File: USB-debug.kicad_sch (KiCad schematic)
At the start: 44 parts, among them J4 USB-C_GCT_USB4105-GF-A, Q25 BSS138PW, Q4 BSS138PW, U16 TPD4E05U06QDQARQ1, U31 FT4232H_VQFN, Y2 Oscillator_12MHz_ESC_2520MV

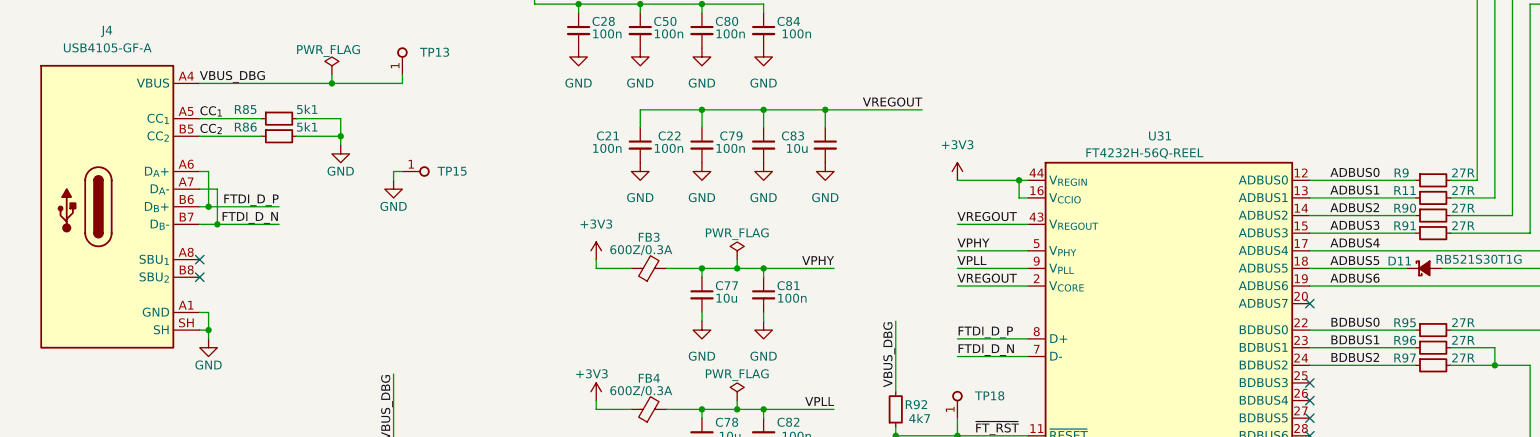
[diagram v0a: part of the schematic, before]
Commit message: Bump to KiCad 9.x
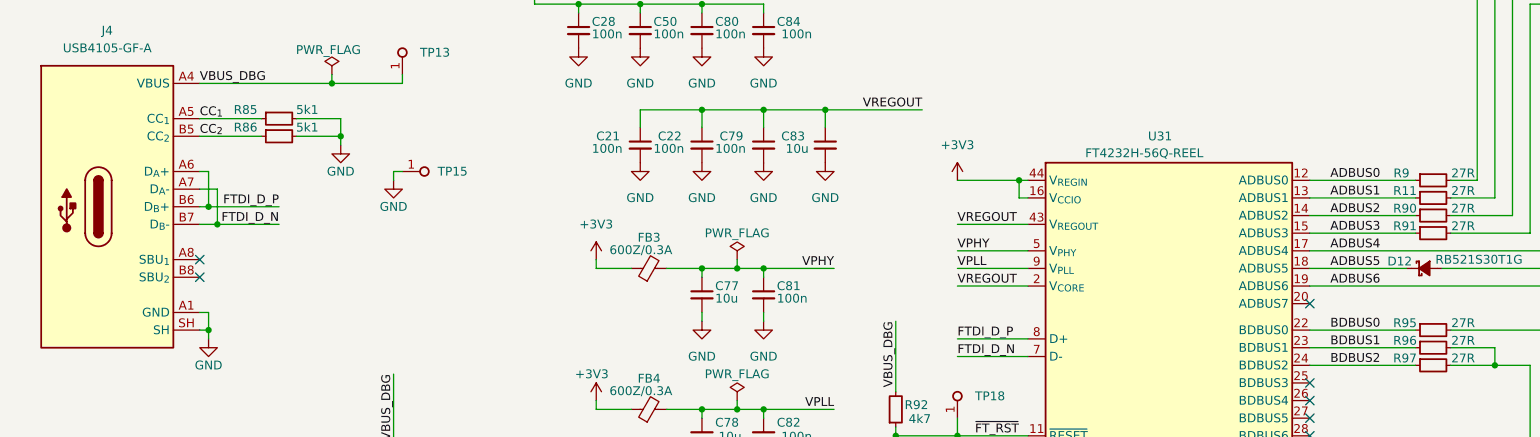
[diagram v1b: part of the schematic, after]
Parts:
- renumbered D11 to D12
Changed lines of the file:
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@@
 (kicad_sch
-	(version 20231120)
+	(version 20250114)
 	(generator "eeschema")
-	(generator_version "8.0")
+	(generator_version "9.0")
 	(paper "A4")
 	(title_block
@@
 		(rev "1.0.0")
 	)
+	(text "FTDI"
+		(exclude_from_sim no)
+		(at 182.626 21.082 0)
+		(effects
+			(font
+				(size 2.54 2.54)
+				(thickness 0.508)
+				(bold yes)
+			)
+		)
+	)
+	(text "Debug USB-C Connector"
+		(exclude_from_sim no)
+		(at 45.466 22.352 0)
+		(effects
+			(font
+				(size 2.54 2.54)
+				(thickness 0.508)
+				(bold yes)
+			)
+		)
+	)
 	(junction
 		(at 115.57 113.03)
@@
 		)
 	)
-	(text "FTDI"
-		(exclude_from_sim no)
-		(at 182.626 21.082 0)
-		(effects
-			(font
-				(size 2.54 2.54)
-				(thickness 0.508)
-				(bold yes)
-			)
-		)
-	)
-	(text "Debug USB-C Connector"
-		(exclude_from_sim no)
-		(at 45.466 22.352 0)
-		(effects
-			(font
-				(size 2.54 2.54)
-				(thickness 0.508)
-				(bold yes)
-			)
-		)
-	)
 	(label "FTDI_D_P"
 		(at 55.88 62.23 180)
-		(fields_autoplaced yes)
 		(effects
 			(font
@@
 	(label "FTDI_D_N"
 		(at 55.88 64.77 180)
-		(fields_autoplaced yes)
 		(effects
 			(font
@@
 	(label "FTDI_D_P"
 		(at 21.59 105.41 0)
-		(fields_autoplaced yes)
 		(effects
 			(font
@@
 	(label "IMU.SCL"
 		(at 248.92 99.06 180)
-		(fields_autoplaced yes)
 		(effects
 			(font
@@
 	(label "FTDI_D_N"
 		(at 153.67 83.82 0)
-		(fields_autoplaced yes)
 		(effects
 			(font
@@
 	(label "~{FT_RST}"
 		(at 156.21 95.25 0)
-		(fields_autoplaced yes)
 		(effects
 			(font
@@
 	(label "VBUS_DBG"
 		(at 144.78 78.74 270)
-		(fields_autoplaced yes)
 		(effects
 			(font
@@
 	(label "VREGOUT"
 		(at 153.67 64.77 0)
-		(fields_autoplaced yes)
 		(effects
 			(font
@@
 	(label "VBUS_DBG"
 		(at 44.45 44.45 0)
-		(fields_autoplaced yes)
 		(effects
 			(font
@@
 	(label "VBUS_DBG"
 		(at 72.39 86.36 270)
-		(fields_autoplaced yes)
 		(effects
 			(font
@@
 	(label "BDBUS2"
 		(at 214.63 85.09 180)
-		(fields_autoplaced yes)
 		(effects
 			(font
@@
 	(label "ADBUS4"
 		(at 214.63 68.58 180)
-		(fields_autoplaced yes)
 		(effects
 			(font
@@
 	(label "BDBUS1"
 		(at 214.63 82.55 180)
-		(fields_autoplaced yes)
 		(effects
 			(font
@@
 	(label "CC_{2}"
 		(at 44.45 52.07 0)
-		(fields_autoplaced yes)
 		(effects
 			(font
@@
 	(label "VPLL"
 		(at 153.67 71.12 0)
-		(fields_autoplaced yes)
 		(effects
 			(font
@@
 	(label "FTDI_D_N"
 		(at 21.59 107.95 0)
-		(fields_autoplaced yes)
 		(effects
 			(font
@@
 	(label "VPLL"
 		(at 135.89 91.44 180)
-		(fields_autoplaced yes)
 		(effects
 			(font
@@
 	(label "FPGA_SPI.CS"
 		(at 251.46 33.02 180)
-		(fields_autoplaced yes)
 		(effects
 			(font
@@
 	(label "VBUS_DBG"
 		(at 21.59 100.33 0)
-		(fields_autoplaced yes)
 		(effects
 			(font
@@
 	(label "ADBUS6"
 		(at 214.63 73.66 180)
-		(fields_autoplaced yes)
 		(effects
 			(font
@@
 	(label "FTDI_D_P"
 		(at 153.67 81.28 0)
-		(fields_autoplaced yes)
 		(effects
 			(font
@@
 	(label "ADBUS0"
 		(at 214.63 58.42 180)
-		(fields_autoplaced yes)
 		(effects
 			(font
@@
 	(label "VPHY"
 		(at 135.89 71.12 180)
-		(fields_autoplaced yes)
 		(effects
 			(font
@@
 	(label "OSCI"
 		(at 153.67 113.03 0)
-		(fields_autoplaced yes)
 		(effects
 			(font
@@
 	(label "VREGOUT"
 		(at 148.59 48.26 180)
-		(fields_autoplaced yes)
 		(effects
 			(font
@@
 	(label "VPHY"
 		(at 153.67 68.58 0)
-		(fields_autoplaced yes)
 		(effects
 			(font
@@
 	(label "CC_{1}"
 		(at 44.45 49.53 0)
-		(fields_autoplaced yes)
 		(effects
 			(font
@@
 	(label "VREGOUT"
 		(at 153.67 73.66 0)
-		(fields_autoplaced yes)
 		(effects
 			(font
@@
 	(label "ADBUS2"
 		(at 214.63 63.5 180)
-		(fields_autoplaced yes)
 		(effects
 			(font
@@
 	(label "ADBUS5"
 		(at 214.63 71.12 180)
-		(fields_autoplaced yes)
 		(effects
 			(font
@@
 	(label "BDBUS0"
 		(at 214.63 80.01 180)
-		(fields_autoplaced yes)
 		(effects
 			(font
@@
 	(label "IMU.SDA"
 		(at 248.92 101.6 180)
-		(fields_autoplaced yes)
 		(effects
 			(font
@@
 	(label "ADBUS3"
 		(at 214.63 66.04 180)
-		(fields_autoplaced yes)
 		(effects
 			(font
@@
 	(label "FPGA_SPI.MOSI"
 		(at 251.46 27.94 180)
-		(fields_autoplaced yes)
 		(effects
 			(font
@@
 	(label "ADBUS1"
 		(at 214.63 60.96 180)
-		(fields_autoplaced yes)
 		(effects
 			(font
@@
 	(label "FPGA_SPI.MISO"
 		(at 251.46 30.48 180)
-		(fields_autoplaced yes)
 		(effects
 			(font
@@
 	(label "FPGA_SPI.SCK"
 		(at 251.46 25.4 180)
-		(fields_autoplaced yes)
 		(effects
 			(font
@@
 		(shape bidirectional)
 		(at 255.27 92.71 0)
-		(fields_autoplaced yes)
 		(effects
 			(font
@@
 		(shape output)
 		(at 255.27 67.31 0)
-		(fields_autoplaced yes)
 		(effects
 			(font
@@
 		(shape bidirectional)
 		(at 255.27 19.05 0)
-		(fields_autoplaced yes)
 		(effects
 			(font
@@
 		(shape input)
 		(at 255.27 63.5 0)
-		(fields_autoplaced yes)
 		(effects
 			(font
@@
 		(shape output)
 		(at 255.27 36.83 0)
-		(fields_autoplaced yes)
 		(effects
 			(font
@@
 		(on_board yes)
 		(dnp no)
-		(property "Reference" "D11"
+		(property "Reference" "D12"
 			(at 217.424 70.104 0)
 			(effects
@@
 		(on_board yes)
 		(dnp no)
-		(property "Reference" "#FLG01"
+		(property "Reference" "#FLG0101"
 			(at 63.5 41.275 0)
 			(effects
